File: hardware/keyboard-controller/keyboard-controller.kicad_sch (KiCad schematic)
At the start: 34 parts, among them J1 Keybed_Connector, J2 Debug_Pins, J3 Barrel_Jack_Switch, J4 CV_OUT, J5 GATE_OUT, U1 L78L09_TO92, U2 LM358, U3 74HC164, U4 74HC164, U5 LM1117-3.3, U6 Pico, U7 TL431LP, U8 MCP4921

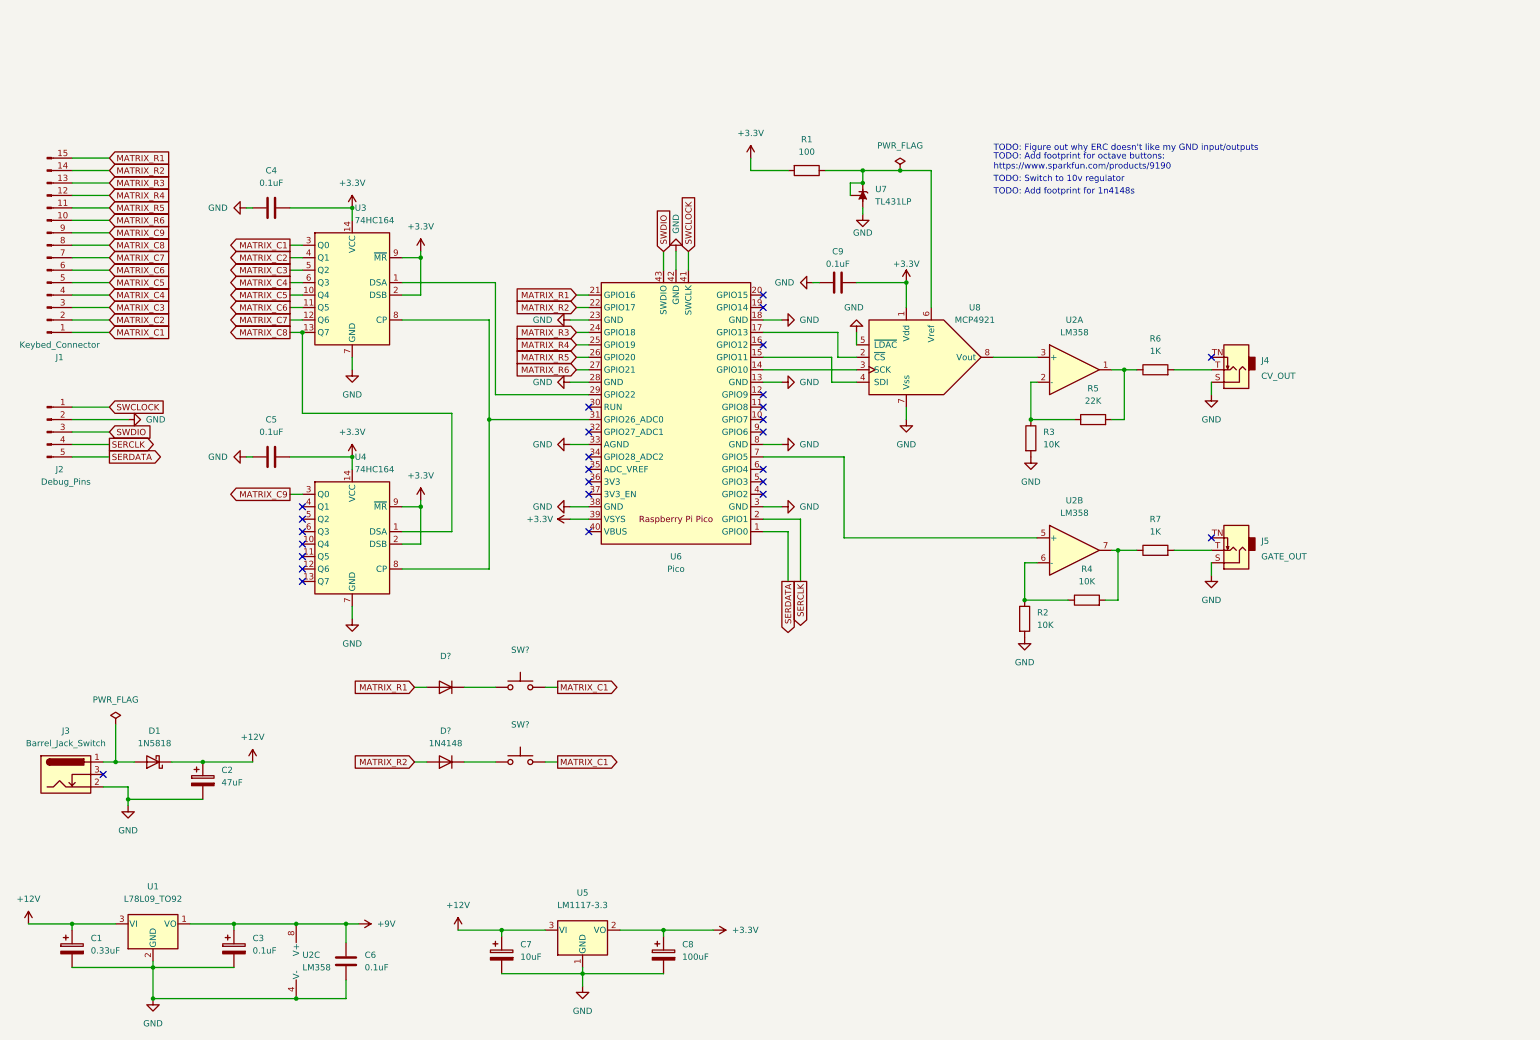
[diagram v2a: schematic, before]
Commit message: Tidied schematic
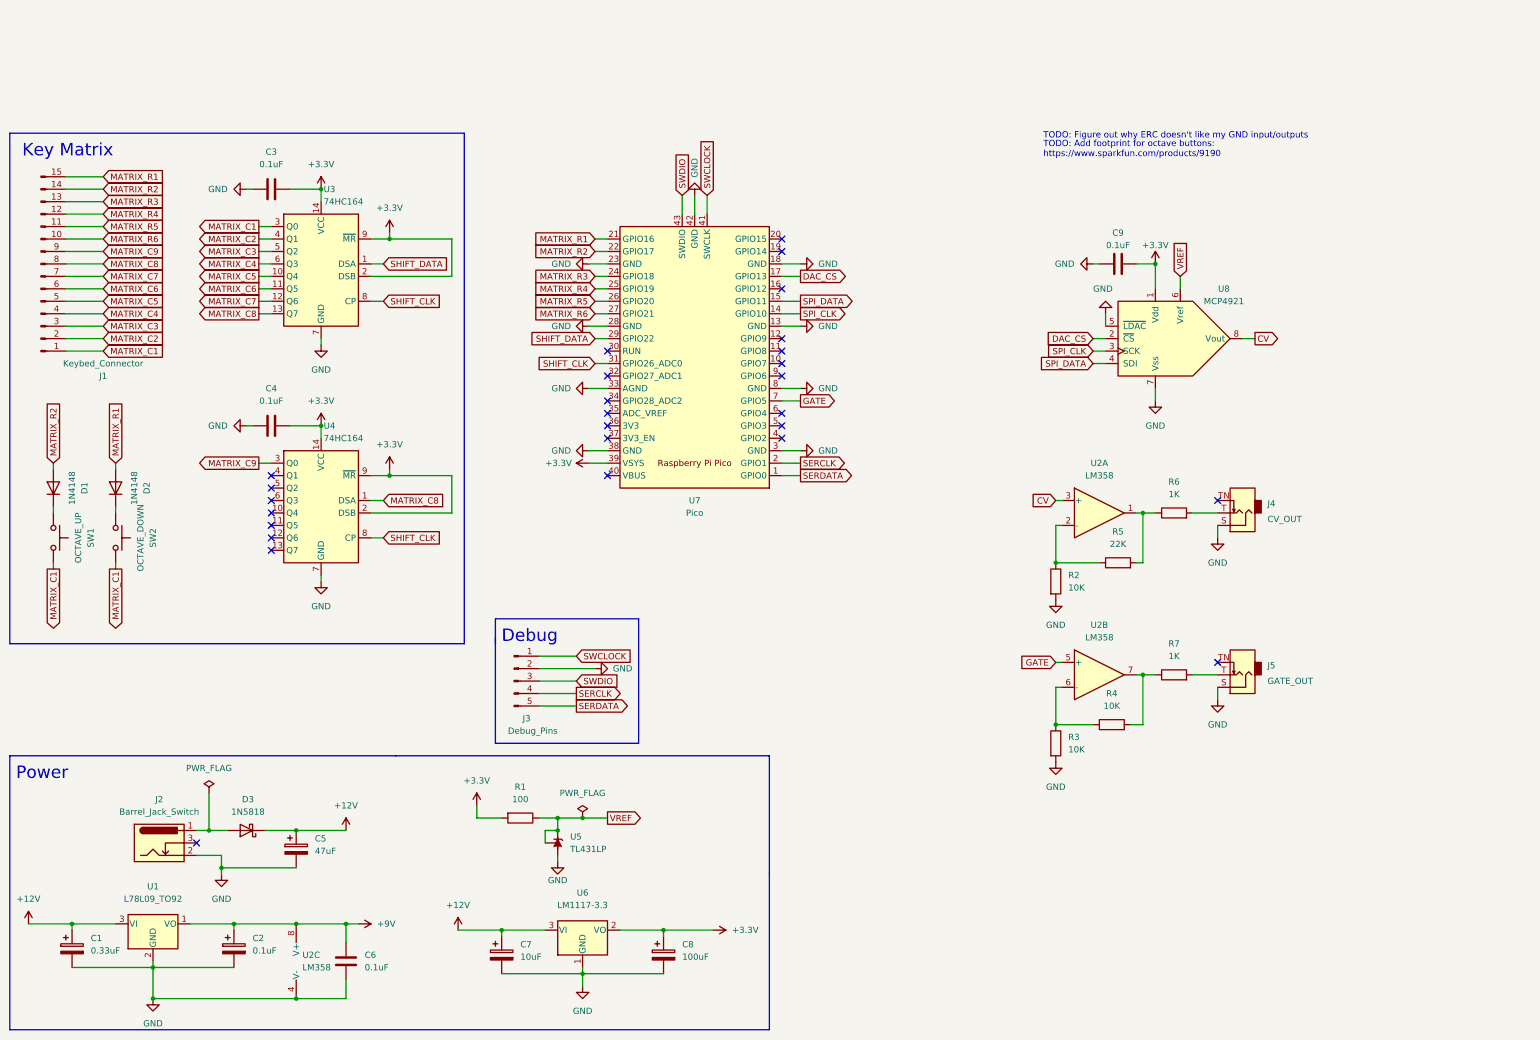
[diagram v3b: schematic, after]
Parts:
- removed C4: 0.1uF, AEC_Capacitors:C_Disc_D5.0mm_W2.5mm_P3.0mm, symbol Device:C
- removed U7: TL431LP, Package_TO_SOT_THT:TO-92_Inline, symbol Reference_Voltage:TL431LP
- added C3: 0.1uF, AEC_Capacitors:C_Disc_D5.0mm_W2.5mm_P3.0mm, symbol Device:C
- added U5: TL431LP, Package_TO_SOT_THT:TO-92_Inline, symbol Reference_Voltage:TL431LP
- D2: renamed from D?; value (none) -> 1N4148; footprint (none) -> Diode_THT:D_DO-35_SOD27_P7.62mm_Horizontal
- SW1: renamed from SW?; value (none) -> OCTAVE_UP
- SW2: renamed from SW?; value (none) -> OCTAVE_DOWN
- gave numbers to parts that had none: 1
- renumbered C3 to C2, C5 to C4, C2 to C5, D1 to D3, J3 to J2, J2 to J3, R3 to R2, R2 to R3, U5 to U6, U6 to U7
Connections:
- net +3V3: now also C3.2
- net GND: now also C3.1, U5.2 (A)
- net GATE: now reaches U2.5 (+), U7.7 (GPIO5)
- net SPI_CLK: now reaches U7.14 (GPIO10), U8.3 (SCK)
- net SPI_DATA: now reaches U7.15 (GPIO11), U8.4 (SDI)
- net DAC_CS: now reaches U7.17 (GPIO13), U8.2 (~{CS})
- net SHIFT_DATA: now reaches U3.1 (DSA), U7.29 (GPIO22)
- net SHIFT_CLK: now reaches U3.8 (CP), U4.8 (CP), U7.31 (GPIO26_ADC0)
- net VREF: now reaches R1.1, U8.6 (Vref)
- net VREF: now also U5.1 (REF), U5.3 (K)
- net CV: now reaches U2.3 (+), U8.8 (Vout)
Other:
- note added: "Debug"
- note added: "Key Matrix"
- note added: "Power"
- note removed: "TODO: Add footprint for 1n4148s"
- note removed: "TODO: Switch to 10v regulator"
- moved on the sheet: C4, C5, C9, D1, D2, D3, J1, J2, J3, J4, J5, R2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

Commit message: Added more IO
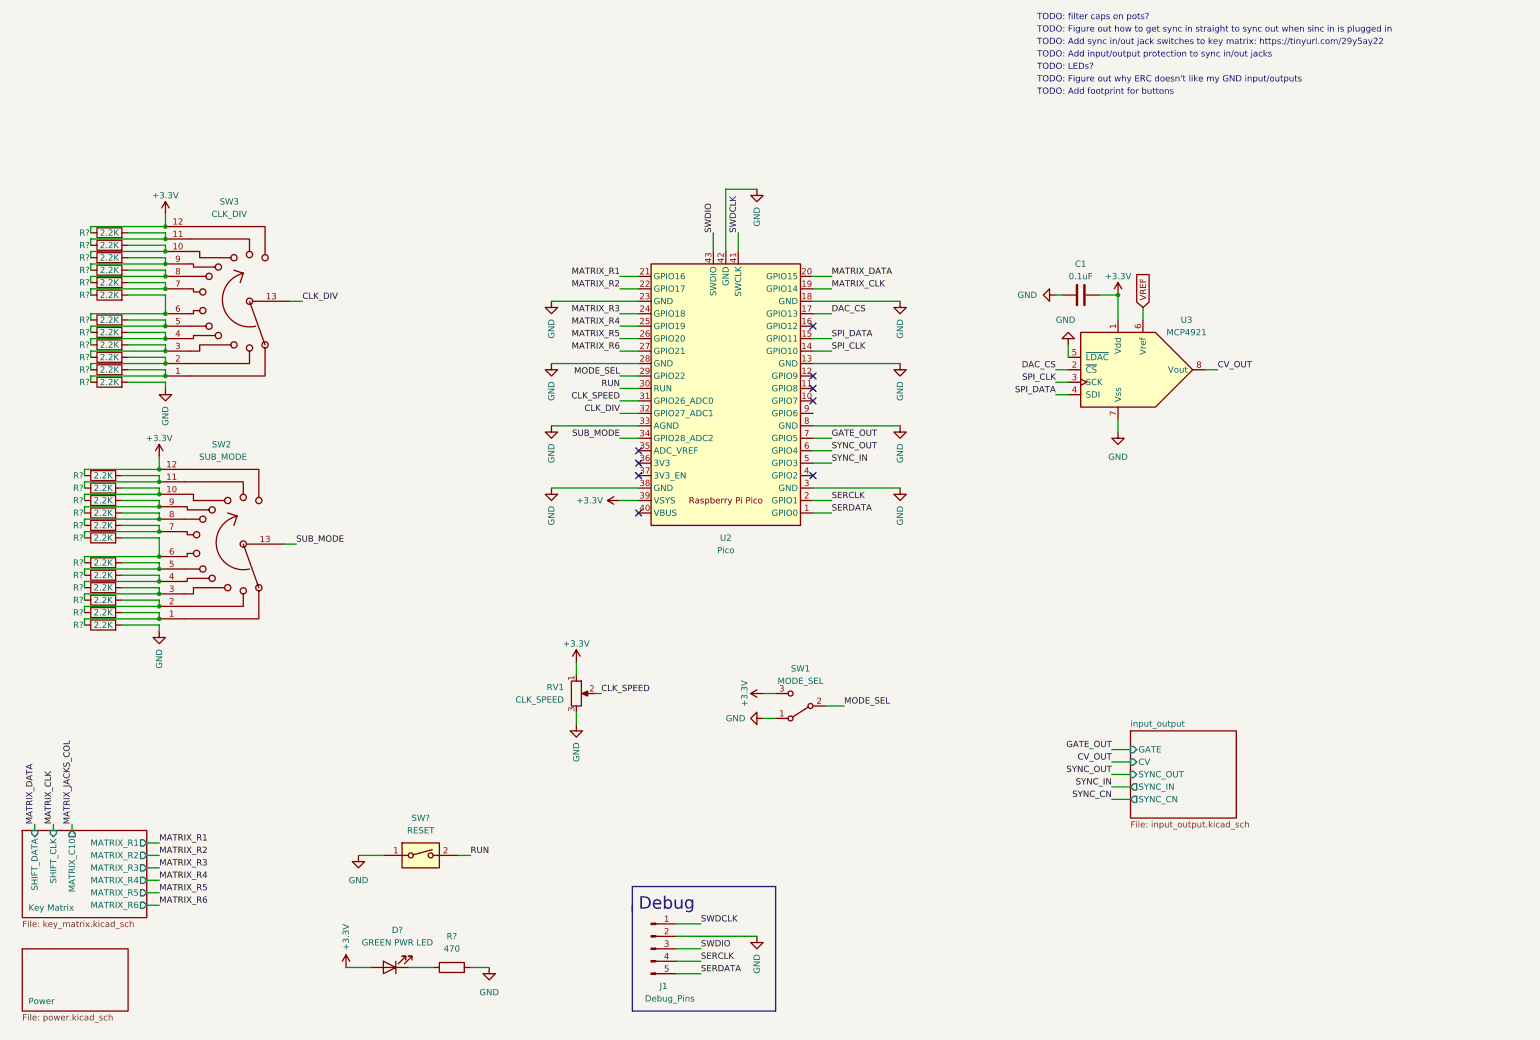
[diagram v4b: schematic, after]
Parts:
- removed C1: 0.33uF, Capacitor_THT:CP_Radial_Tantal_D4.5mm_P2.50mm, symbol Device:C_Polarized
- removed C2: 0.1uF, Capacitor_THT:CP_Radial_Tantal_D4.5mm_P2.50mm, symbol Device:C_Polarized
- removed C3, C4, C6: 0.1uF, AEC_Capacitors:C_Disc_D5.0mm_W2.5mm_P3.0mm, symbol Device:C
- removed C5: 47uF, Capacitor_THT:CP_Radial_D5.0mm_P2.00mm, symbol Device:C_Polarized
- removed C7: 10uF, Capacitor_THT:CP_Radial_Tantal_D4.5mm_P2.50mm, symbol Device:C_Polarized
- removed C8: 100uF, Capacitor_THT:CP_Radial_Tantal_D4.5mm_P2.50mm, symbol Device:C_Polarized
- removed D1, D2: 1N4148, Diode_THT:D_DO-35_SOD27_P7.62mm_Horizontal, symbol Diode:1N4148
- removed D3: 1N5818, Diode_THT:D_DO-41_SOD81_P10.16mm_Horizontal, symbol Diode:1N5818
- removed J1: Keybed_Connector, Connector_IDC:IDC-Header_2x08_P2.54mm_Vertical, symbol Connector:Conn_01x15_Male
- removed J2: Barrel_Jack_Switch, WEALTH_METAL_Barrel_Jacks:BarrelJack_Horizontal_2.1mm_WEALTH_METAL, symbol Connector:Barrel_Jack_Switch
- removed J4: CV_OUT, AudioJacks:Jack_3.5mm_QingPu_WQP-PJ398SM_Vertical, symbol Connector:AudioJack2_SwitchT
- removed J5: GATE_OUT, AudioJacks:Jack_3.5mm_QingPu_WQP-PJ398SM_Vertical, symbol Connector:AudioJack2_SwitchT
- removed R1: 100, Royal_Ohm_Resistors:R_Axial_DIN0207_L6.8mm_D2.5mm_P10.16mm_Horizontal, symbol Device:R
- removed R2, R3, R4: 10K, Royal_Ohm_Resistors:R_Axial_DIN0207_L6.8mm_D2.5mm_P10.16mm_Horizontal, symbol Device:R
- removed R5: 22K, Royal_Ohm_Resistors:R_Axial_DIN0207_L6.8mm_D2.5mm_P10.16mm_Horizontal, symbol Device:R
- removed R6, R7: 1K, Royal_Ohm_Resistors:R_Axial_DIN0207_L6.8mm_D2.5mm_P10.16mm_Horizontal, symbol Device:R
- removed SW1: OCTAVE_UP, symbol Switch:SW_Push
- removed SW2: OCTAVE_DOWN, symbol Switch:SW_Push
- removed U1: L78L09_TO92, Package_TO_SOT_THT:TO-92_Inline, symbol Regulator_Linear:L78L09_TO92
- removed U2: LM358, Package_DIP:DIP-8_W7.62mm_Socket, symbol Amplifier_Operational:LM358
- removed U3, U4: 74HC164, Package_DIP:DIP-14_W7.62mm_Socket, symbol 74xx:74HC164
- removed U5: TL431LP, Package_TO_SOT_THT:TO-92_Inline, symbol Reference_Voltage:TL431LP
- removed U6: LM1117-3.3, Package_TO_SOT_THT:TO-220-3_Horizontal_TabDown, symbol Regulator_Linear:LM1117-3.3
- added D?: GREEN PWR LED, symbol Device:LED
- added R? (x24): 2.2K, symbol Device:R
- added R?: 470, symbol Device:R
- added RV1: CLK_SPEED, symbol Device:R_Potentiometer
- added SW1: MODE_SEL, symbol Switch:SW_SPDT
- added SW2: SUB_MODE, symbol Switch:SW_Rotary12
- added SW3: CLK_DIV, symbol Switch:SW_Rotary12
- added SW?: RESET, symbol Switch:SW_DIP_x01
- C1: renamed from C9; Manufacturer (none) -> AEC; Manufacturer Part No. (none) -> 0.1uF 50V Ceramic Disc Capacitor; Supplier (none) -> Tayda; Supplier Part No. (none) -> A-4008
- J1: renamed from J3; Supplier (none) -> Tayda
- renumbered U7 to U2, U8 to U3
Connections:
- net +3V3: now also D?.2 (A), R?.1, R?.1, RV1.1, SW1.3 (C), SW2.12, SW3.12
- net GND: now also R?.2, R?.2, R?.2, RV1.3, SW1.1 (A), SW?.1
- net MATRIX_CLK: now reaches U2.19 (GPIO14)
- net MATRIX_DATA: now reaches U2.20 (GPIO15)
- net RUN: now reaches U2.30 (RUN)
- net RUN: now also SW?.2
- net CLK_DIV: now reaches U2.32 (GPIO27_ADC1)
- net CLK_DIV: now also SW3.13
- net SUB_MODE: now reaches U2.34 (GPIO28_ADC2)
- net SUB_MODE: now also SW2.13
- net SYNC_IN: now reaches U2.5 (GPIO3)
- net SYNC_OUT: now reaches U2.6 (GPIO4)
- net CV renamed CV_OUT
- net GATE renamed GATE_OUT
- net SHIFT_CLK renamed CLK_SPEED
- net CLK_SPEED: now also RV1.2
- net SHIFT_DATA renamed MODE_SEL
- net MODE_SEL: now also SW1.2 (B)
- net SWCLOCK renamed SWDCLK
- new net: D?.1 (K), R?.1
- new net: R?.1, R?.2, SW3.2
- new net: R?.1, R?.2, SW3.1
- new net: R?.1, R?.2, SW3.4
- new net: R?.1, R?.2, SW3.3
- new net: R?.1, R?.2, SW2.4
- new net: R?.1, R?.2, SW2.3
- new net: R?.1, R?.2, SW2.8
- new net: R?.1, R?.2, SW2.7
- new net: R?.1, R?.2, SW3.6
- new net: R?.1, R?.2, SW3.5
- new net: R?.1, R?.2, SW2.9
- new net: R?.1, R?.2, SW2.11
- new net: R?.1, R?.2, SW3.11
- new net: R?.1, R?.2, SW3.10
- new net: R?.1, R?.2, SW3.8
- new net: R?.1, R?.2, SW3.7
- new net: R?.1, R?.2, SW2.6
- new net: R?.1, R?.2, SW2.5
- new net: R?.1, R?.2, SW3.9
- new net: R?.1, R?.2, SW2.1
- new net: R?.1, R?.2, SW2.2
- new net: R?.1, R?.2, SW2.10
- no-connect marks 27 -> 9
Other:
- added sheet Key Matrix (key_matrix.kicad_sch)
- added sheet Power (power.kicad_sch)
- added sheet input_output (input_output.kicad_sch)
- note added: "TODO: Add footprint for buttons"
- note added: "TODO: Add input/output protection to sync in/out jacks"
- note added: "TODO: Add sync in/out jack switches to key matrix: https://tinyurl.com/29y5ay22"
- note added: "TODO: Figure out how to get sync in straight to sync out when sinc in is plugged in"
- note added: "TODO: LEDs?"
- note added: "TODO: filter caps on pots?"
- note removed: "Key Matrix"
- note removed: "Power"
- note removed: "TODO: Add footprint for octave buttons: https://www.sparkfun.com/products/9190"
- moved on the sheet: C1, J1, U2, U3
